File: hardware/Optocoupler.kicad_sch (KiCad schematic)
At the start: 6 parts, among them U5 VOH1016AB-T2

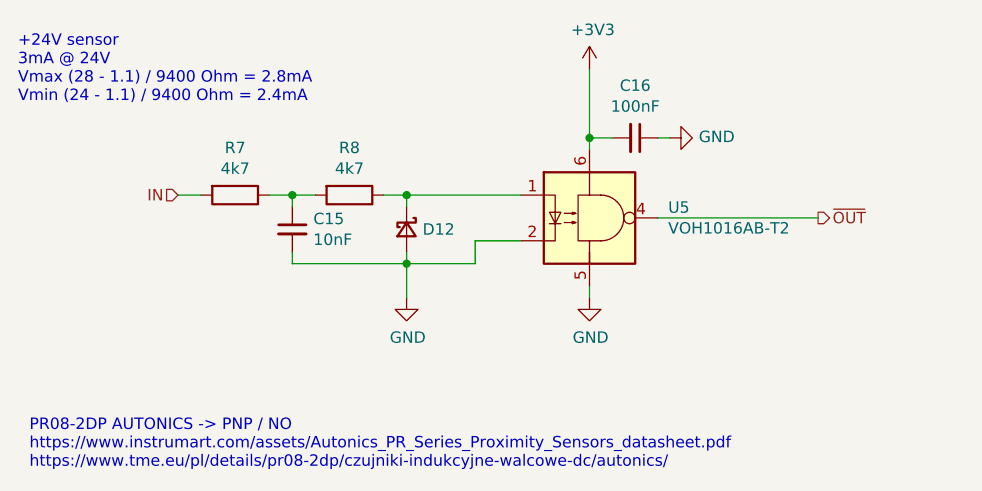
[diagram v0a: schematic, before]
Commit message: changed clock and 5v converter coils, footprints rearrange commponets to fit the need now the board connector is vertical not horizontal relative to the pcb's longest side
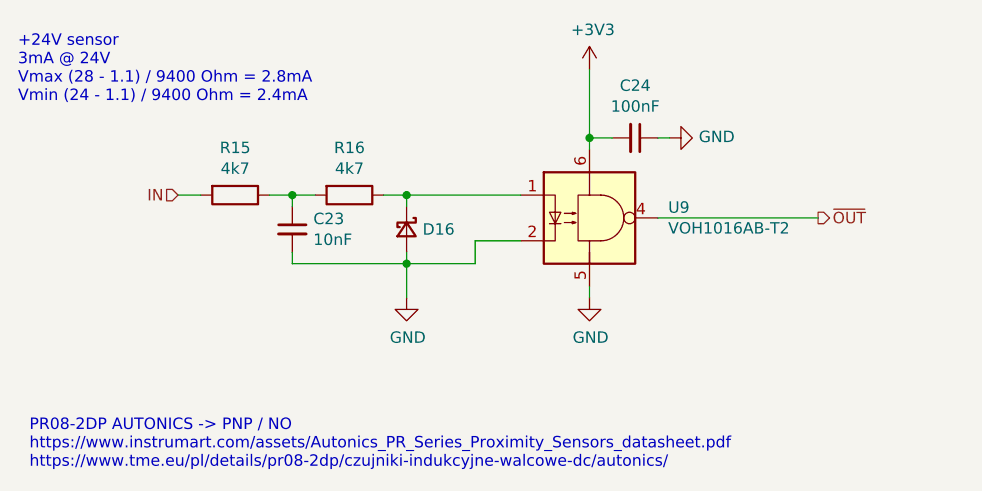
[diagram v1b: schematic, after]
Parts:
- renumbered C15 to C23, C16 to C24, D12 to D16, R7 to R15, R8 to R16, U5 to U9
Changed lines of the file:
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@@
   (symbol (lib_id "Isolator:H11L2") (at 168.91 105.41 0)
     (in_bom yes) (on_board yes)
-    (property "Reference" "U5" (id 0) (at 177.6476 104.2416 0)
+    (property "Reference" "U9" (id 0) (at 177.6476 104.2416 0)
       (effects (font (size 1.27 1.27)) (justify left))
     )
@@
   (symbol (lib_id "Device:R") (at 142.24 102.87 270)
     (in_bom yes) (on_board yes)
-    (property "Reference" "R8" (id 0) (at 142.24 97.6122 90))
+    (property "Reference" "R16" (id 0) (at 142.24 97.6122 90))
     (property "Value" "4k7" (id 1) (at 142.24 99.9236 90))
     (property "Footprint" "Resistor_SMD:R_0603_1608Metric" (id 2) (at 142.24 101.092 90)
@@
   (symbol (lib_id "Device:C_Small") (at 135.89 106.68 0)
     (in_bom yes) (on_board yes)
-    (property "Reference" "C15" (id 0) (at 138.2268 105.5116 0)
+    (property "Reference" "C23" (id 0) (at 138.2268 105.5116 0)
       (effects (font (size 1.27 1.27)) (justify left))
     )
@@
   (symbol (lib_id "power:GND") (at 168.91 114.3 0)
     (in_bom yes) (on_board yes)
-    (property "Reference" "#PWR033" (id 0) (at 168.91 120.65 0)
+    (property "Reference" "#PWR049" (id 0) (at 168.91 120.65 0)
       (effects (font (size 1.27 1.27)) hide)
     )
@@
   (symbol (lib_id "power:+3V3") (at 168.91 88.9 0)
     (in_bom yes) (on_board yes)
-    (property "Reference" "#PWR032" (id 0) (at 168.91 92.71 0)
+    (property "Reference" "#PWR048" (id 0) (at 168.91 92.71 0)
       (effects (font (size 1.27 1.27)) hide)
     )
@@
   (symbol (lib_id "Device:C_Small") (at 173.99 96.52 270)
     (in_bom yes) (on_board yes)
-    (property "Reference" "C16" (id 0) (at 173.99 90.7034 90))
+    (property "Reference" "C24" (id 0) (at 173.99 90.7034 90))
     (property "Value" "100nF" (id 1) (at 173.99 93.0148 90))
     (property "Footprint" "Capacitor_SMD:C_0603_1608Metric" (id 2) (at 173.99 96.52 0)
@@
   (symbol (lib_id "power:GND") (at 177.8 96.52 90)
     (in_bom yes) (on_board yes)
-    (property "Reference" "#PWR034" (id 0) (at 184.15 96.52 0)
+    (property "Reference" "#PWR050" (id 0) (at 184.15 96.52 0)
       (effects (font (size 1.27 1.27)) hide)
     )
@@
   (symbol (lib_id "Device:D_Schottky_Small") (at 148.59 106.68 270)
     (in_bom yes) (on_board yes)
-    (property "Reference" "D12" (id 0) (at 150.368 106.68 90)
+    (property "Reference" "D16" (id 0) (at 150.368 106.68 90)
       (effects (font (size 1.27 1.27)) (justify left))
     )
@@
   (symbol (lib_id "Device:R") (at 129.54 102.87 270)
     (in_bom yes) (on_board yes)
-    (property "Reference" "R7" (id 0) (at 129.54 97.6122 90))
+    (property "Reference" "R15" (id 0) (at 129.54 97.6122 90))
     (property "Value" "4k7" (id 1) (at 129.54 99.9236 90))
     (property "Footprint" "Resistor_SMD:R_0603_1608Metric" (id 2) (at 129.54 101.092 90)
@@
   (symbol (lib_id "power:GND") (at 148.59 114.3 0)
     (in_bom yes) (on_board yes)
-    (property "Reference" "#PWR031" (id 0) (at 148.59 120.65 0)
+    (property "Reference" "#PWR047" (id 0) (at 148.59 120.65 0)
       (effects (font (size 1.27 1.27)) hide)
     )

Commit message: minor improvements
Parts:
- renumbered C23 to C21, C24 to C22, D16 to D15, R15 to R13, R16 to R14, U9 to U8
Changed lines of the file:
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@@
   (symbol (lib_id "Isolator:H11L2") (at 168.91 105.41 0)
     (in_bom yes) (on_board yes)
-    (property "Reference" "U9" (id 0) (at 177.6476 104.2416 0)
+    (property "Reference" "U8" (id 0) (at 177.6476 104.2416 0)
       (effects (font (size 1.27 1.27)) (justify left))
     )
@@
       (effects (font (size 1.27 1.27)) hide)
     )
-    (property "Datasheet" "https://pl.mouser.com/datasheet/2/427/VISH_S_A0007770803_1-2570127.pdf" (id 3) (at 166.624 105.41 0)
+    (property "Datasheet" "https://www.onsemi.com/pub/Collateral/H11L3M-D.PDF" (id 3) (at 166.624 105.41 0)
       (effects (font (size 1.27 1.27)) hide)
     )
@@
   (symbol (lib_id "Device:R") (at 142.24 102.87 270)
     (in_bom yes) (on_board yes)
-    (property "Reference" "R16" (id 0) (at 142.24 97.6122 90))
+    (property "Reference" "R14" (id 0) (at 142.24 97.6122 90))
     (property "Value" "4k7" (id 1) (at 142.24 99.9236 90))
     (property "Footprint" "Resistor_SMD:R_0603_1608Metric" (id 2) (at 142.24 101.092 90)
@@
   (symbol (lib_id "Device:C_Small") (at 135.89 106.68 0)
     (in_bom yes) (on_board yes)
-    (property "Reference" "C23" (id 0) (at 138.2268 105.5116 0)
+    (property "Reference" "C21" (id 0) (at 138.2268 105.5116 0)
       (effects (font (size 1.27 1.27)) (justify left))
     )
@@
   (symbol (lib_id "power:GND") (at 168.91 114.3 0)
     (in_bom yes) (on_board yes)
-    (property "Reference" "#PWR049" (id 0) (at 168.91 120.65 0)
+    (property "Reference" "#PWR045" (id 0) (at 168.91 120.65 0)
       (effects (font (size 1.27 1.27)) hide)
     )
@@
   (symbol (lib_id "power:+3V3") (at 168.91 88.9 0)
     (in_bom yes) (on_board yes)
-    (property "Reference" "#PWR048" (id 0) (at 168.91 92.71 0)
+    (property "Reference" "#PWR044" (id 0) (at 168.91 92.71 0)
       (effects (font (size 1.27 1.27)) hide)
     )
@@
   (symbol (lib_id "Device:C_Small") (at 173.99 96.52 270)
     (in_bom yes) (on_board yes)
-    (property "Reference" "C24" (id 0) (at 173.99 90.7034 90))
+    (property "Reference" "C22" (id 0) (at 173.99 90.7034 90))
     (property "Value" "100nF" (id 1) (at 173.99 93.0148 90))
     (property "Footprint" "Capacitor_SMD:C_0603_1608Metric" (id 2) (at 173.99 96.52 0)
@@
   (symbol (lib_id "power:GND") (at 177.8 96.52 90)
     (in_bom yes) (on_board yes)
-    (property "Reference" "#PWR050" (id 0) (at 184.15 96.52 0)
+    (property "Reference" "#PWR046" (id 0) (at 184.15 96.52 0)
       (effects (font (size 1.27 1.27)) hide)
     )
@@
   (symbol (lib_id "Device:D_Schottky_Small") (at 148.59 106.68 270)
     (in_bom yes) (on_board yes)
-    (property "Reference" "D16" (id 0) (at 150.368 106.68 90)
+    (property "Reference" "D15" (id 0) (at 150.368 106.68 90)
       (effects (font (size 1.27 1.27)) (justify left))
     )
@@
   (symbol (lib_id "Device:R") (at 129.54 102.87 270)
     (in_bom yes) (on_board yes)
-    (property "Reference" "R15" (id 0) (at 129.54 97.6122 90))
+    (property "Reference" "R13" (id 0) (at 129.54 97.6122 90))
     (property "Value" "4k7" (id 1) (at 129.54 99.9236 90))
     (property "Footprint" "Resistor_SMD:R_0603_1608Metric" (id 2) (at 129.54 101.092 90)
@@
   (symbol (lib_id "power:GND") (at 148.59 114.3 0)
     (in_bom yes) (on_board yes)
-    (property "Reference" "#PWR047" (id 0) (at 148.59 120.65 0)
+    (property "Reference" "#PWR043" (id 0) (at 148.59 120.65 0)
       (effects (font (size 1.27 1.27)) hide)
     )
